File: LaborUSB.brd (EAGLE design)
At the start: 97 x 47 mm, 8 parts

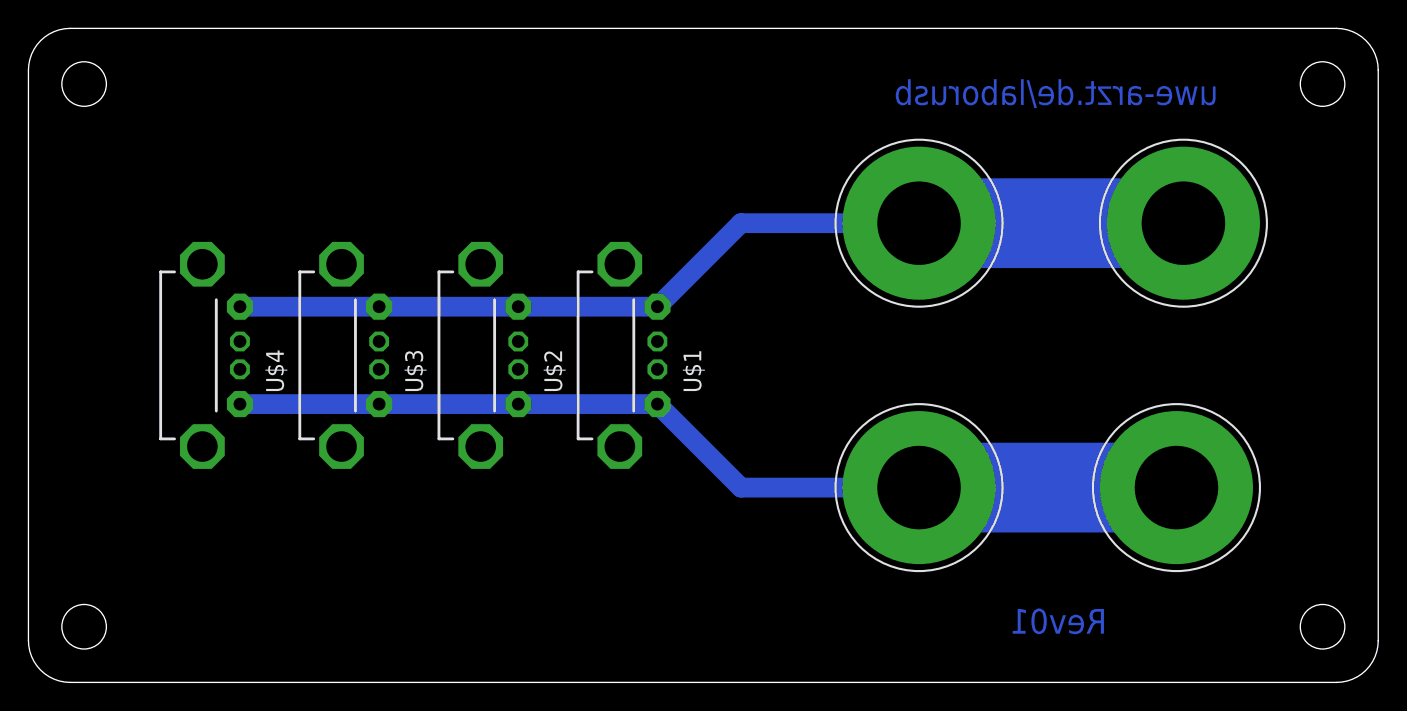
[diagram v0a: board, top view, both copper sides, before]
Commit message: Added iPhone charge capabilty, Component Names
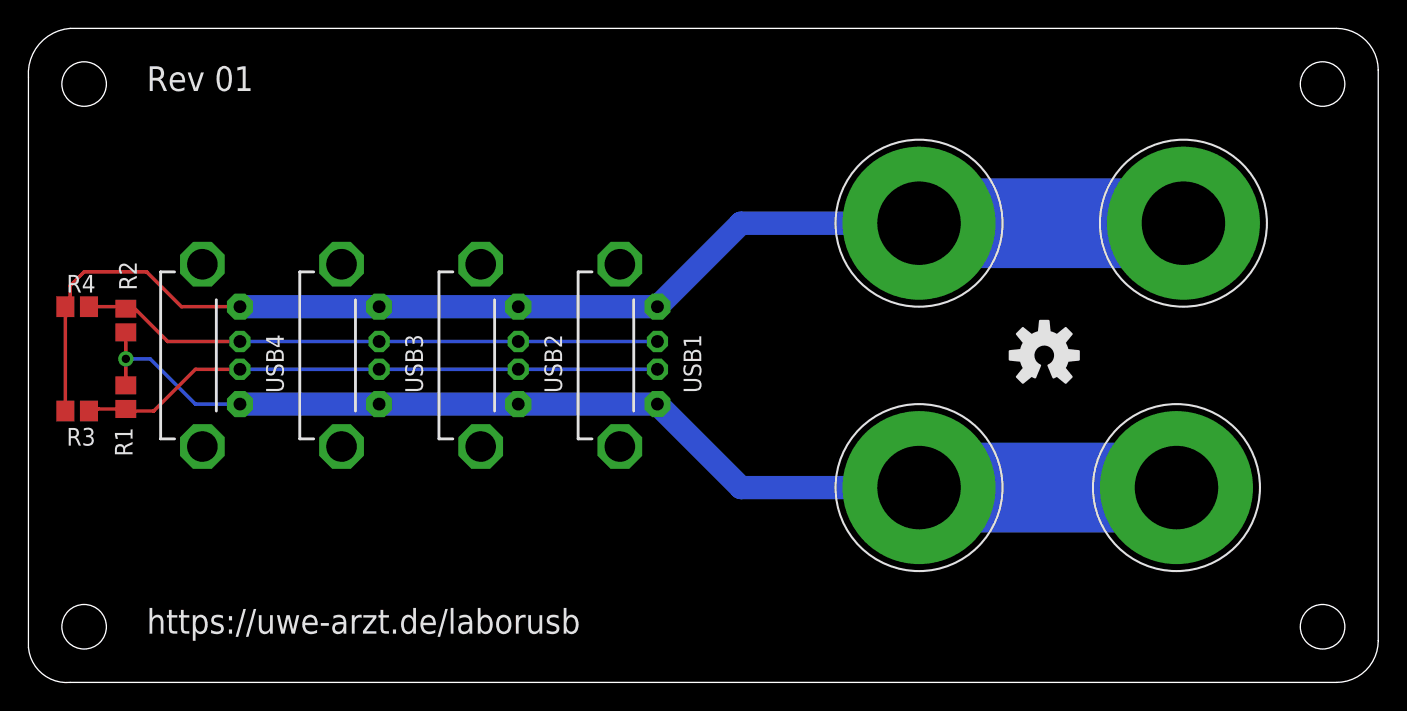
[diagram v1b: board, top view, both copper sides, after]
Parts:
- added LOGO1: OSHW-LOGOM, SparkFun-Aesthetics:OSHW-LOGO-M
- added R1: 43K, resistor:R0805
- added R2: 75K, resistor:R0805
- added R3, R4: 51K, resistor:R0805
- renumbered U$1 to USB1, U$2 to USB2, U$3 to USB3, U$4 to USB4
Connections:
- new net D+: R2.1, R4.2, USB1.D+, USB2.D+, USB3.D+, USB4.D+
- new net D-: R1.1, R3.2, USB1.D-, USB2.D-, USB3.D-, USB4.D-
- net GND: now also R3.1, R4.1
- net VBUS: now also R1.2, R2.2
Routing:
- net D-: track 0.00 -> 42.6 mm
- net D+: track 0.00 -> 41.9 mm
- net GND: track 70.3 -> 93.1 mm
- net VBUS: track 69.8 -> 83.1 mm, vias 0 -> 1
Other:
- outline, holes or cut-outs redrawn
- board text added: "Rev 01"
- board text added: "https://uwe-arzt.de/laborusb"
- board text removed: "Rev01"
- board text removed: "uwe-arzt.de/laborusb"

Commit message: First prototype order
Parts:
- renumbered J1 to GND
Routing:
- net GND: track 93.1 -> 22.8 mm
- net VBUS: track 83.1 -> 13.3 mm
- added copper zone on layer 16, net GND
- added copper zone on layer 16, net VBUS
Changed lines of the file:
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@@
 </autorouter>
 <elements>
-<element name="J1" library="LaborUSB" package="BANANA" value="" x="64" y="33"/>
+<element name="GND" library="LaborUSB" package="BANANA" value="" x="64" y="33"/>
 <element name="J2" library="LaborUSB" package="BANANA" value="" x="83" y="33"/>
 <element name="J3" library="LaborUSB" package="BANANA" value="" x="64" y="14"/>
@@
 <signals>
 <signal name="GND">
-<contactref element="J1" pad="P$1"/>
+<contactref element="GND" pad="P$1"/>
 <contactref element="J2" pad="P$1"/>
 <contactref element="USB2" pad="GND"/>
@@
 <contactref element="USB4" pad="GND"/>
 <contactref element="USB3" pad="GND"/>
-<wire x1="15.2" y1="27" x2="25.2" y2="27" width="1.6764" layer="16"/>
-<wire x1="25.2" y1="27" x2="35.2" y2="27" width="1.6764" layer="16"/>
-<wire x1="35.2" y1="27" x2="45.2" y2="27" width="1.6764" layer="16"/>
-<wire x1="45.2" y1="27" x2="51.2" y2="33" width="1.6764" layer="16"/>
-<wire x1="51.2" y1="33" x2="64" y2="33" width="1.6764" layer="16"/>
-<wire x1="64" y1="33" x2="83" y2="33" width="6.4516" layer="16"/>
 <contactref element="R3" pad="1"/>
 <contactref element="R4" pad="1"/>
@@
 <wire x1="3" y1="28.5" x2="3" y2="27.35" width="0.254" layer="1"/>
 <wire x1="3" y1="27.35" x2="2.65" y2="27" width="0.254" layer="1"/>
+<polygon width="0.4064" layer="16">
+<vertex x="14" y="26"/>
+<vertex x="90" y="26"/>
+<vertex x="90" y="43"/>
+<vertex x="14" y="43"/>
+</polygon>
 </signal>
 <signal name="VBUS">
@@
 <contactref element="USB4" pad="VBUS"/>
 <contactref element="USB3" pad="VBUS"/>
-<wire x1="15.2" y1="20" x2="25.2" y2="20" width="1.6764" layer="16"/>
-<wire x1="25.2" y1="20" x2="35.2" y2="20" width="1.6764" layer="16"/>
-<wire x1="35.2" y1="20" x2="45.2" y2="20" width="1.6764" layer="16"/>
-<wire x1="45.2" y1="20" x2="51.2" y2="14" width="1.6764" layer="16"/>
-<wire x1="51.2" y1="14" x2="64" y2="14" width="1.6764" layer="16"/>
-<wire x1="64" y1="14" x2="82.5" y2="14" width="6.4516" layer="16"/>
 <contactref element="R1" pad="2"/>
 <contactref element="R2" pad="2"/>
@@
 <wire x1="12" y1="20" x2="8.75" y2="23.25" width="0.254" layer="16"/>
 <wire x1="8.75" y1="23.25" x2="7" y2="23.25" width="0.254" layer="16"/>
+<polygon width="0.4064" layer="16">
+<vertex x="14" y="21"/>
+<vertex x="90" y="21"/>
+<vertex x="90" y="4"/>
+<vertex x="14" y="4"/>
+</polygon>
 </signal>
 <signal name="D+">

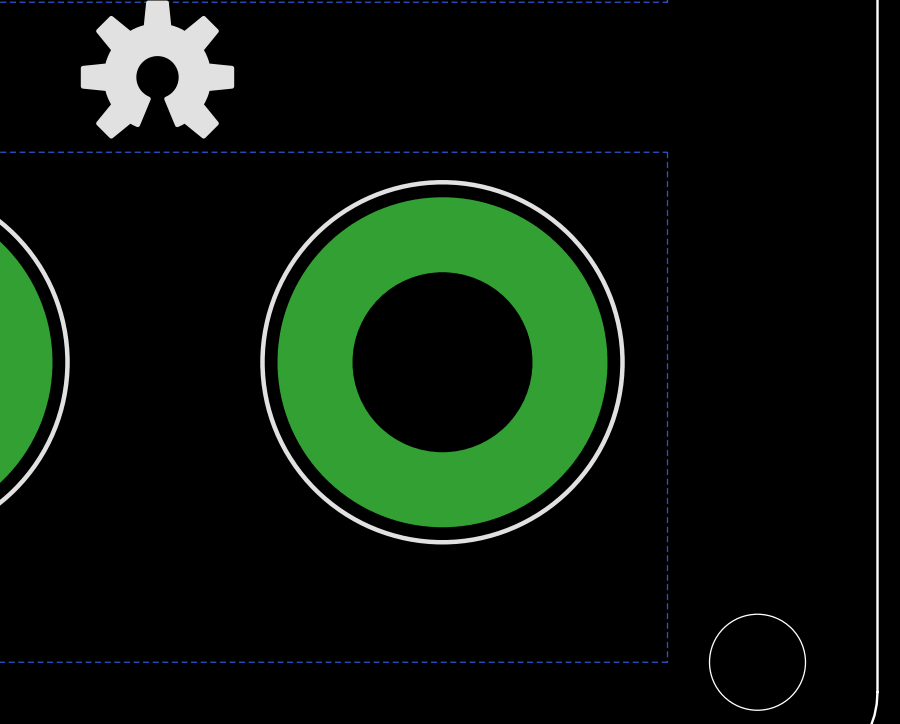
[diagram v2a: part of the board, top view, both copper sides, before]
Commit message: Fix in thermals on Banana Plug
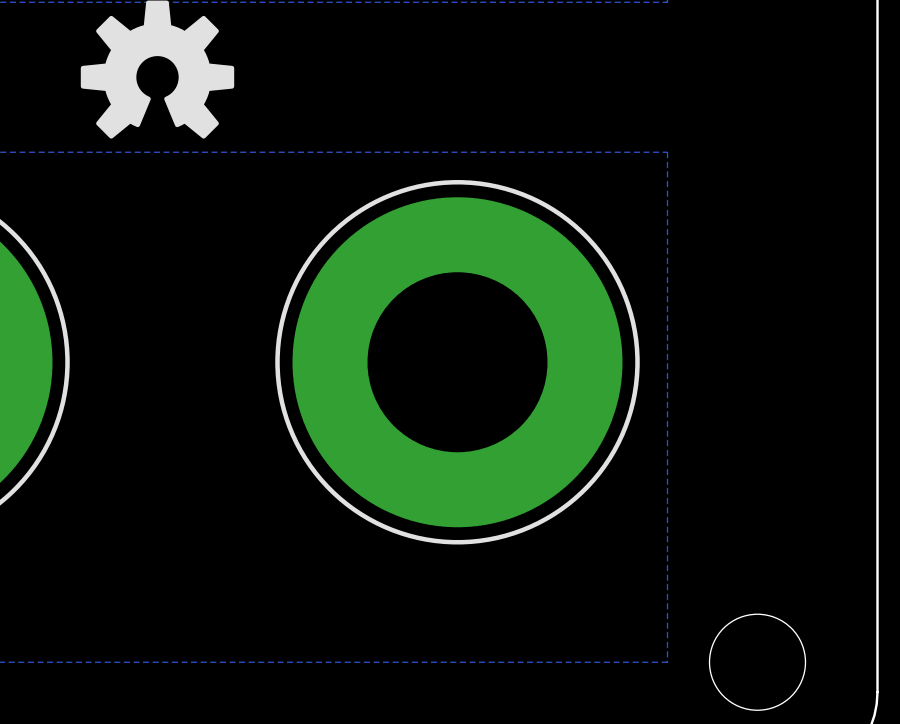
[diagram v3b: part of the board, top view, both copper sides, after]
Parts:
- moved J4 0.50 mm to (83.0, 14.0)
- renumbered GND to J1
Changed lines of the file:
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@@
 </autorouter>
 <elements>
-<element name="GND" library="LaborUSB" package="BANANA" value="" x="64" y="33"/>
-<element name="J2" library="LaborUSB" package="BANANA" value="" x="83" y="33"/>
-<element name="J3" library="LaborUSB" package="BANANA" value="" x="64" y="14"/>
-<element name="J4" library="LaborUSB" package="BANANA" value="" x="82.5" y="14"/>
 <element name="USB1" library="LaborUSB" package="USB-A-VERTICAL" value="USB+SHIELD" x="42.5" y="23.5"/>
 <element name="USB2" library="LaborUSB" package="USB-A-VERTICAL" value="USB+SHIELD" x="32.5" y="23.5"/>
@@
 <element name="R4" library="resistor" package="R0805" value="51K" x="3.5" y="27"/>
 <element name="LOGO1" library="SparkFun-Aesthetics" package="OSHW-LOGO-M" value="OSHW-LOGOM" x="73" y="23.5"/>
+<element name="J1" library="LaborUSB" package="BANANA" value="" x="64" y="33"/>
+<element name="J2" library="LaborUSB" package="BANANA" value="" x="83" y="33"/>
+<element name="J3" library="LaborUSB" package="BANANA" value="" x="64" y="14"/>
+<element name="J4" library="LaborUSB" package="BANANA" value="" x="83" y="14"/>
 </elements>
 <signals>
 <signal name="GND">
-<contactref element="GND" pad="P$1"/>
-<contactref element="J2" pad="P$1"/>
 <contactref element="USB2" pad="GND"/>
 <contactref element="USB1" pad="GND"/>
@@
 <vertex x="14" y="43"/>
 </polygon>
+<contactref element="J1" pad="P$1"/>
+<contactref element="J2" pad="P$1"/>
 </signal>
 <signal name="VBUS">
-<contactref element="J3" pad="P$1"/>
-<contactref element="J4" pad="P$1"/>
 <contactref element="USB2" pad="VBUS"/>
 <contactref element="USB1" pad="VBUS"/>
@@
 <vertex x="14" y="4"/>
 </polygon>
+<contactref element="J3" pad="P$1"/>
+<contactref element="J4" pad="P$1"/>
 </signal>
 <signal name="D+">
